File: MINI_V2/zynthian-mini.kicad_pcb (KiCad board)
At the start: 2 copper layers, 163 x 120 mm, 91 parts, among them J1 NEUTRIK, J2 NEUTRIK, J3 Conn_02x04_Odd_Even, J4 Conn_01x05, J6 TRRS-PJ-320A, SW1 SW_Push, SW10 SW_Push, SW11 SW_Push, SW12 SW_Push, SW13 SW_Push, SW14 SW_Push, SW15 SW_Push, SW16 SW_Push, SW17 SW_Push, SW18 SW_Push, SW19 SW_Push, SW2 SW_Push, SW20 SW_Push, SW3 SW_Push, SW4 SW_Push, SW5 SW_Push, SW6 SW_Push, SW7 SW_Push, SW8 SW_Push, SW9 SW_Push, U1 74HCT14, U2 H11L1M

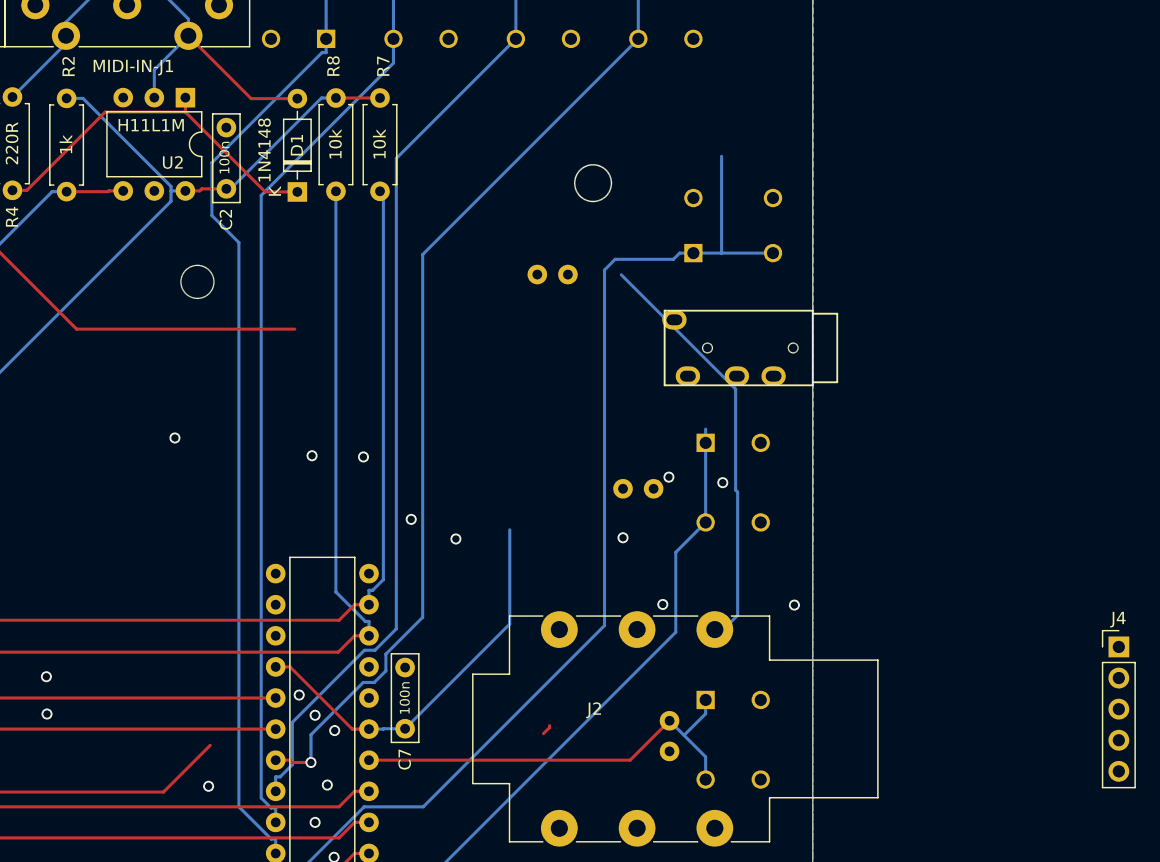
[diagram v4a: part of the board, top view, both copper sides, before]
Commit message: finished schematic, added headphones jack
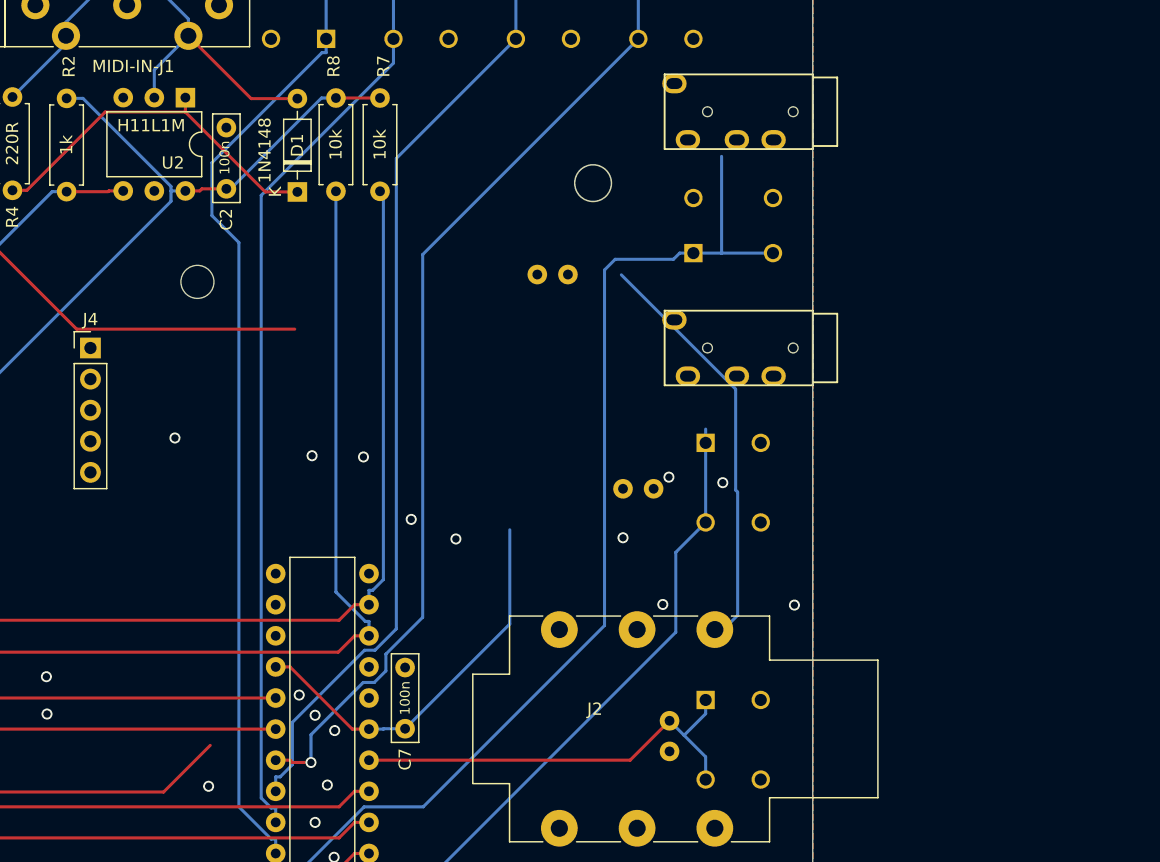
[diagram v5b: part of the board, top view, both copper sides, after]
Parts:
- added J7: TRRS-PJ-320A, project-footprints:TRRS-PJ-320A, F.Cu at (196.4, 55.6)
- moved J4 87.5 mm to (137.4, 74.9)
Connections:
- J4 pad 1: unconnected-(J4-Pin_1-Pad1) -> Net-(J4-Pin_1)
- J4 pad 2: unconnected-(J4-Pin_2-Pad2) -> GND
- J4 pad 3: unconnected-(J4-Pin_3-Pad3) -> Net-(J4-Pin_3)
- J4 pad 4: unconnected-(J4-Pin_4-Pad4) -> GND
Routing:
- net AUDIO_L_MINUS: track 0.86 -> 0.00 mm

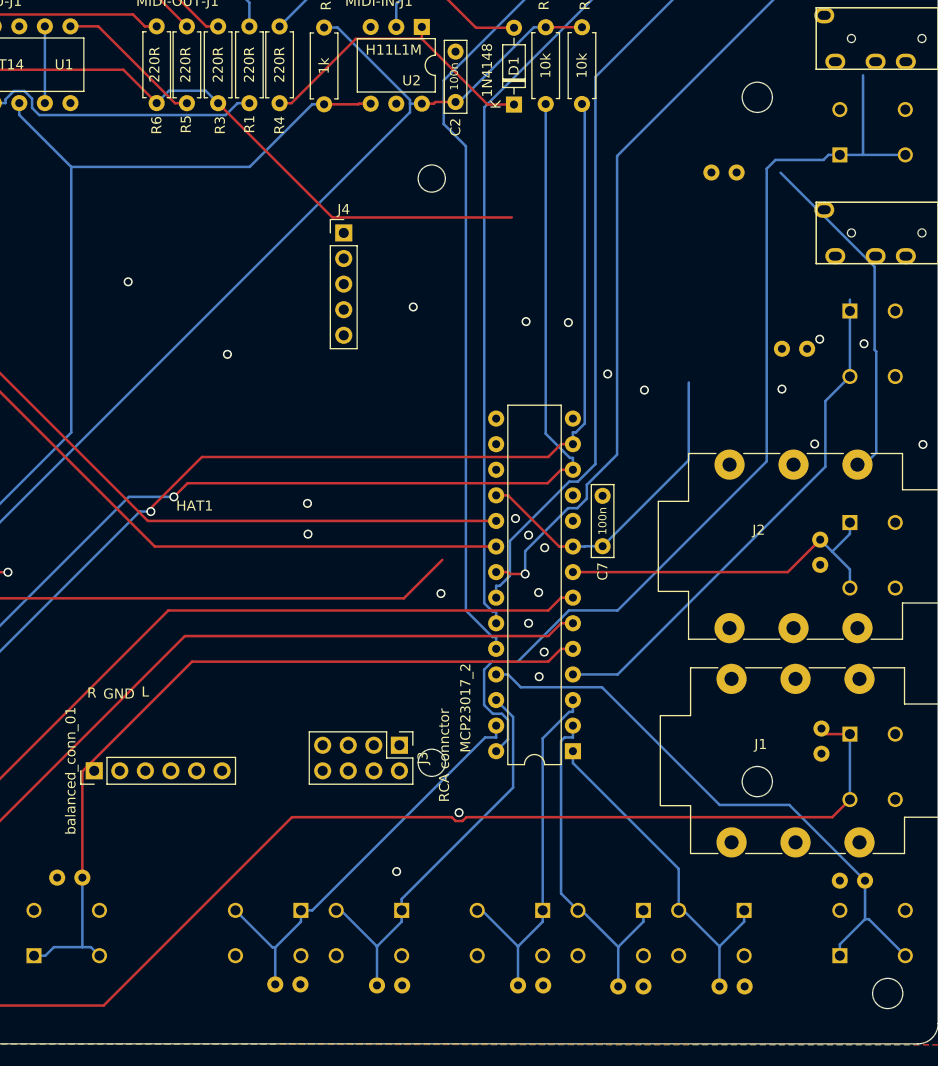
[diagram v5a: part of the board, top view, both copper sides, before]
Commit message: finished all tracks, but pins not aligned
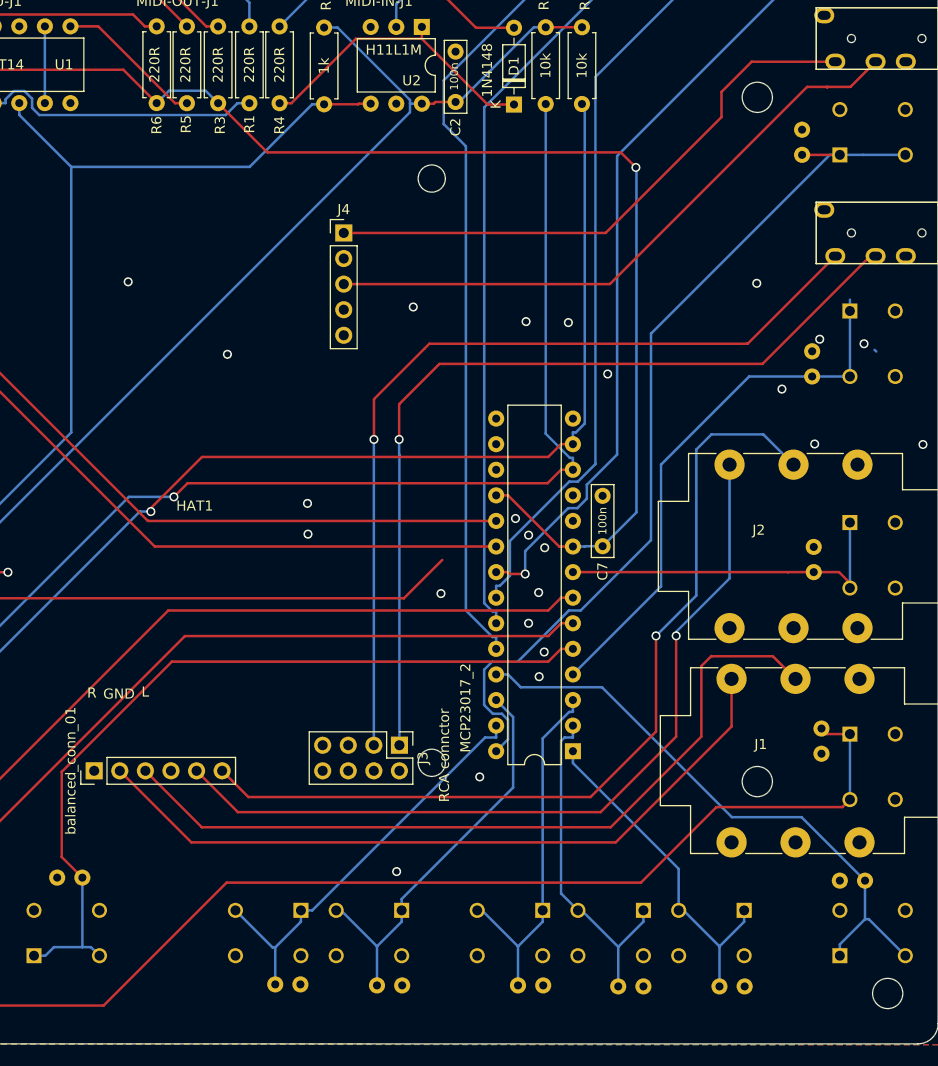
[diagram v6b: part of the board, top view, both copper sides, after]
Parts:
- moved C11 6.73 mm to (182.9, 67.1), turned to 90 degrees
- moved C23 3.29 mm to (184.1, 108.5), turned to 90 degrees
- moved C17 2.80 mm to (183.9, 89.1), turned to 90 degrees
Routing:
- net AUDIO_R_MINUS: track 0.59 -> 88.6 mm, vias 0 -> 1
- net Net-(J3-Pin_1): track 0.00 -> 87.3 mm, vias 0 -> 1
- net Net-(J3-Pin_3): track 0.00 -> 86.0 mm, vias 0 -> 1
- net AUDIO_R_PLUS: track 0.00 -> 81.6 mm, vias 0 -> 1
- net AUDIO_L_MINUS: track 0.00 -> 78.9 mm
- net AUDIO_L_PLUS: track 0.00 -> 73.2 mm
- net Net-(J4-Pin_3): track 0.00 -> 62.0 mm
- net Net-(J4-Pin_1): track 0.00 -> 57.3 mm
- net GND: track 118.1 -> 84.3 mm
- net +5V: track 238.4 -> 267.9 mm, vias 0 -> 1
- net SWITCH-8: track 98.0 -> 88.8 mm
- net SWITCH-12: track 51.2 -> 54.8 mm
- net SWITCH-13: track 78.4 -> 81.3 mm

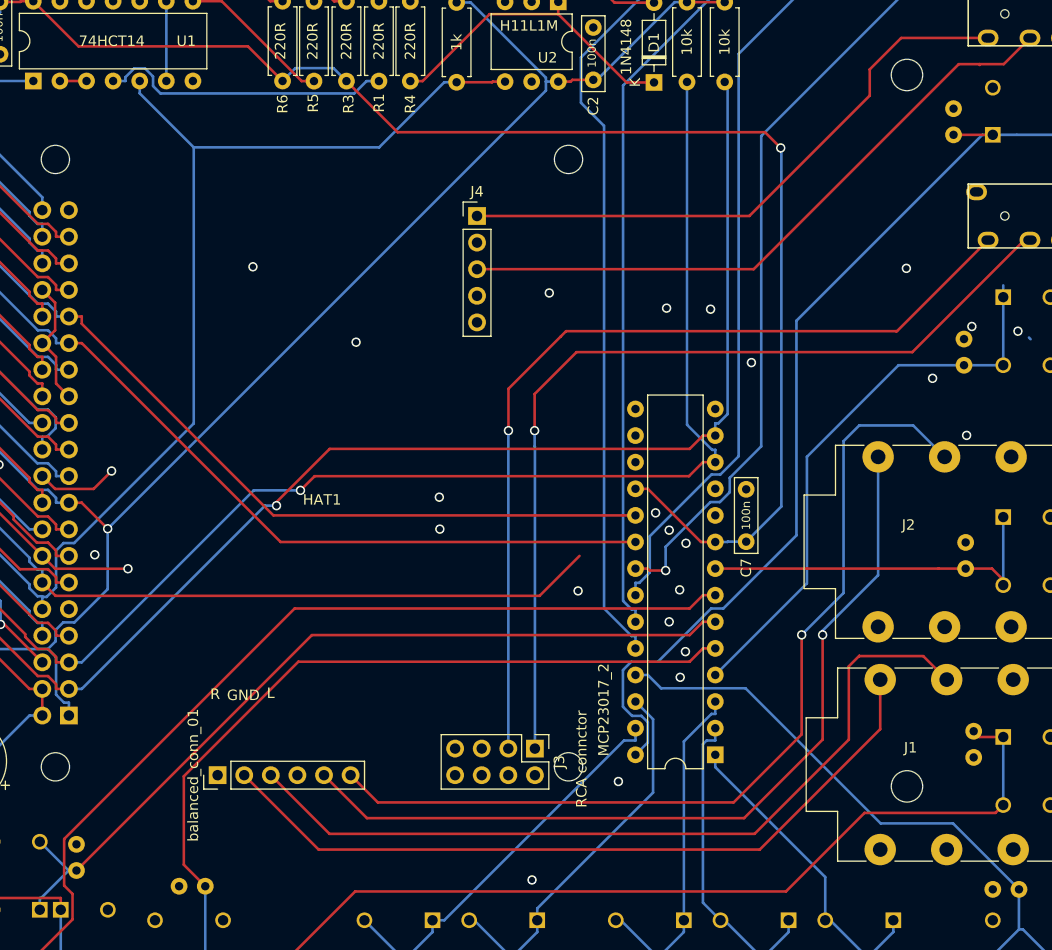
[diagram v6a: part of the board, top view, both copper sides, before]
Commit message: aligned connectors, rerouted; scree hole is covered by L-bal jack
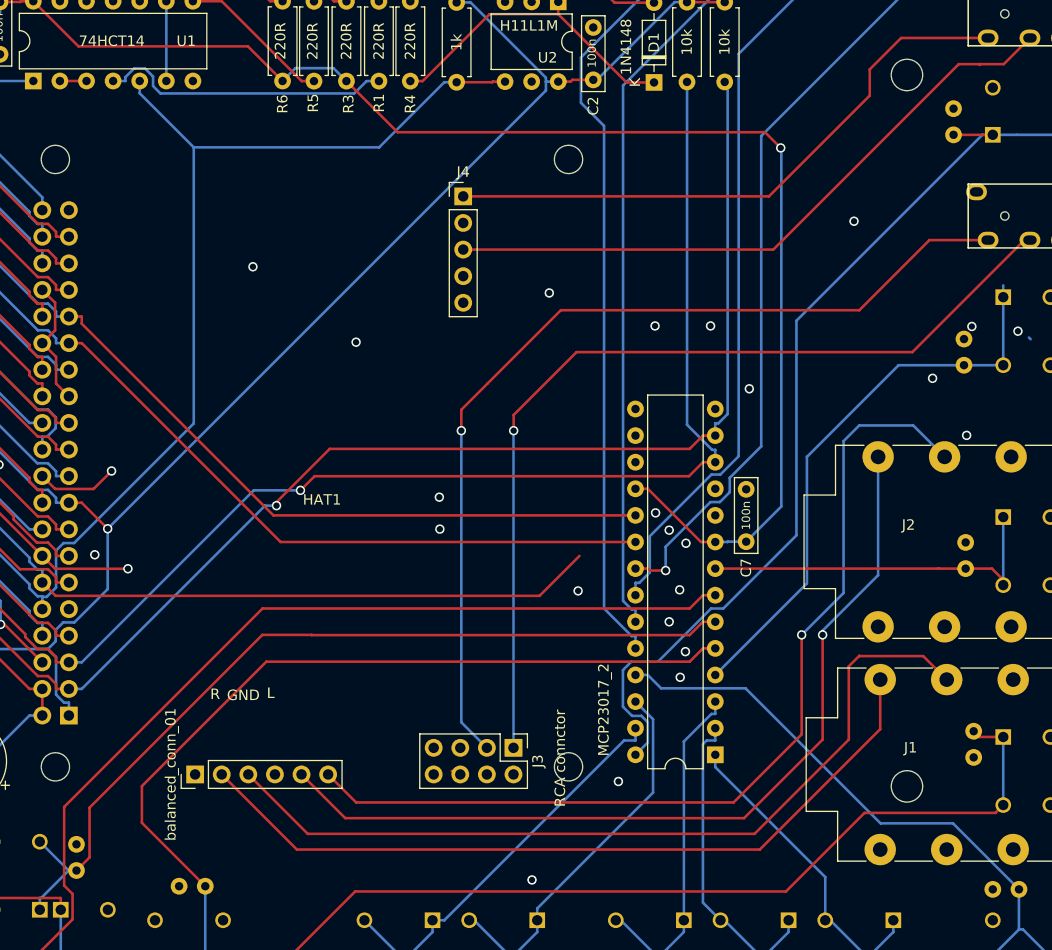
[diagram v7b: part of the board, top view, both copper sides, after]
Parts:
- moved logo1 16.2 mm to (121.0, 81.8)
- moved REF** 14.7 mm to (120.2, 73.8)
- moved J4 2.29 mm to (136.1, 73.0)
- moved balanced_conn_01 2.15 mm to (110.5, 128.2)
- moved J3 2.05 mm to (140.9, 125.7)
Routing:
- net SWITCH-13: track 81.3 -> 86.4 mm
- net Net-(J3-Pin_3): track 86.0 -> 90.3 mm
- net SWITCH-14: track 80.4 -> 83.2 mm
- net AUDIO_R_MINUS: track 88.6 -> 90.8 mm
- net AUDIO_L_PLUS: track 73.2 -> 75.3 mm
- net AUDIO_L_MINUS: track 78.9 -> 81.1 mm
- net AUDIO_R_PLUS: track 81.6 -> 83.8 mm
- net SWITCH-15: track 109.7 -> 111.5 mm
- net unconnected-(J3-Pin_8-Pad8): track 0.92 -> 0.00 mm
- net unconnected-(J3-Pin_6-Pad6): track 0.00 -> 0.92 mm
- net Net-(J3-Pin_1): track 87.3 -> 88.0 mm
- net Net-(J4-Pin_1): track 57.3 -> 57.8 mm
- net Net-(J4-Pin_3): track 62.0 -> 62.6 mm
